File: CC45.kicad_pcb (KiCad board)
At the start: 2 copper layers, 247 x 80.8 mm, 130 parts, among them J1 AVR-ISP-6, SW1 RESET, SW10 K08, SW11 K09, SW12 K0A, SW13 K0B, SW14 K0C, SW15 K10, SW16 K11, SW17 K12, SW18 K13, SW19 K14, SW2 K00, SW20 K15, SW21 K16, SW22 K17, SW23 K18, SW24 K19, SW25 K1A, SW26 K1B, SW27 K20, SW28 K21, SW29 K22, SW3 K01, SW30 K23, SW31 K24, SW32 K25, SW33 K26, SW34 K27, SW35 K28, SW36 K29, SW37 K2A, SW38 K2B, SW39 K30, SW4 K02, SW40 K31, SW41 K32, SW42 K33, SW43 K34, SW44 K36, SW45 K38, SW46 K39, SW47 K3A, SW48 K3B, SW5 K03, SW6 K04, SW7 K05, SW8 K06, SW9 K07, U1 ATmega32U4-AU, U2 PRTR5V0U2X, X1 XTAL

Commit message: start adding rgb
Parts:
- removed G***: LOGO, cc:cc
- removed REF** (x5): MountingHole_2.2mm_M2_Pad, MountingHole:MountingHole_2.2mm_M2_Pad
- C1, C2, C3, C4, C5, C6, C7, C8: footprint custom:C_1206_3216Metric_Pad1.42x1.75mm_HandSolder -> Capacitor_SMD:C_1206_3216Metric_Pad1.42x1.75mm_HandSolder
- D1, D10, D11, D12, D13, D14, D15, D16, D17, D18, D19, D2, D20, D21, D22, D23, D24, D25, D26, D27, D28, D29, D3, D30, D31, D32, D33, D34, D35, D36, D37, D38, D39, D4, D40, D41, D42, D43, D44, D45, D46, D47, D5, D6, D7, D8, D9: footprint custom:D_SOD-323_HandSoldering -> Diode_SMD:D_SOD-323_HandSoldering
- R1, R2, R3, R4, R5, R6: footprint custom:R_1206_3216Metric_Pad1.42x1.75mm_HandSolder -> Resistor_SMD:R_1206_3216Metric_Pad1.42x1.75mm_HandSolder
- SW10, SW11, SW12, SW13, SW14, SW16, SW17, SW18, SW19, SW2, SW20, SW21, SW22, SW23, SW24, SW25, SW28, SW29, SW3, SW30, SW31, SW32, SW33, SW34, SW35, SW36, SW37, SW4, SW40 (x2), SW47 (x2), SW5, SW6, SW7, SW8, SW9: footprint MX_19mm:MX_19mm-1U-NoLED -> mx_rgb:ChocMx_Socket
- SW15, SW38, SW41, SW42, SW45: footprint MX_19mm:MX_19mm-1.25U-NoLED -> mx_rgb:ChocMx_Socket
- SW26, SW27, SW43, SW44: footprint MX_19mm:MX_19mm-1.75U-NoLED -> mx_rgb:ChocMx_Socket
- SW39, SW46, SW48: footprint MX_19mm:MX_19mm-1.25U-NoLED -> Button_Switch_Keyboard:SW_Cherry_MX_1.00u_PCB
- SW39, SW46, SW48: footprint MX_19mm:MX_19mm-1.5U-NoLED -> Button_Switch_Keyboard:SW_Cherry_MX_1.00u_PCB
- SW41: footprint MX_19mm:MX_19mm-1.5U-NoLED -> mx_rgb:ChocMx_Socket
- SW43: footprint MX_19mm:MX_19mm-2.25U-ReversedStabilizers-NoLED -> mx_rgb:ChocMx_Socket
- SW44: footprint MX_19mm:MX_19mm-2.75U-ReversedStabilizers-NoLED -> mx_rgb:ChocMx_Socket
- SW44: footprint MX_19mm:MX_19mm-6U-ReversedStabilizers-NoLED -> mx_rgb:ChocMx_Socket
- moved F1 5.29 mm to (156.5, 40.6)
- moved R6 4.01 mm to (152.1, 29.7), turned to 0 degrees
- moved R5 2.58 mm to (162.3, 29.0), turned to -90 degrees
- moved U2 1.39 mm to (158.0, 30.2)
- turned SW40 to 180 degrees
- turned SW8 to 180 degrees
- turned SW9 to 180 degrees
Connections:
- SW1 pad 1: RESET -> GND
- SW1 pad 2: GND -> RESET
- U1 pad 18: Net-(U1-Pad18) -> (no net)
- U1 pad 19: Net-(U1-Pad19) -> (no net)
- U1 pad 20: Net-(U1-Pad20) -> (no net)
- U1 pad 21: Net-(U1-Pad21) -> (no net)
- U1 pad 42: Net-(U1-Pad42) -> (no net)
- U1 pad 8: Net-(U1-Pad8) -> (no net)
- USB1 pad 3: Net-(USB1-Pad3) -> (no net)
- USB1 pad 9: Net-(USB1-Pad9) -> (no net)
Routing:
- net row0: track 404.0 -> 115.7 mm, vias 2 -> 0
- net row1: track 371.5 -> 109.0 mm, vias 2 -> 0
- net col11: track 184.4 -> 32.1 mm, vias 3 -> 0
- net col12: track 157.6 -> 10.4 mm, vias 3 -> 0
- net col10: track 158.8 -> 34.8 mm, vias 3 -> 0
- net col9: track 144.2 -> 38.5 mm, vias 3 -> 0
- net col8: track 125.7 -> 37.9 mm, vias 3 -> 0
- net GND: track 234.2 -> 149.0 mm, vias 2 -> 0
- net +5V: track 208.8 -> 144.5 mm, vias 9 -> 8
- net /USB_P: track 54.1 -> 2.89 mm
- net /USB_N: track 52.8 -> 3.04 mm
- net col6: track 84.8 -> 37.6 mm, vias 5 -> 3
- net col7: track 77.1 -> 33.2 mm
- net col2: track 129.4 -> 85.5 mm
- net col1: track 150.4 -> 106.5 mm
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
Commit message: routing
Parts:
- moved D8 1.78 mm to (174.5, 31.5)
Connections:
- D1 pad 1: row0 -> Net-(D1-Pad1)
- D10 pad 1: row0 -> Net-(D1-Pad1)
- D11 pad 1: row0 -> Net-(D1-Pad1)
- D12 pad 1: row0 -> Net-(D1-Pad1)
- D13 pad 1: row0 -> Net-(D1-Pad1)
- D2 pad 1: row0 -> Net-(D1-Pad1)
- D3 pad 1: row0 -> Net-(D1-Pad1)
- D4 pad 1: row0 -> Net-(D1-Pad1)
- D5 pad 1: row0 -> Net-(D1-Pad1)
- D6 pad 1: row0 -> Net-(D1-Pad1)
- D7 pad 1: row0 -> Net-(D1-Pad1)
- D8 pad 1: row0 -> Net-(D1-Pad1)
- D9 pad 1: row0 -> Net-(D1-Pad1)
- SW10 pad 1: Net-(D9-Pad2) -> Net-(SW10-Pad1)
- SW10 pad 10: (no net) -> Net-(SW10-Pad10)
- SW10 pad 11: (no net) -> Net-(SW10-Pad11)
- SW10 pad 12: (no net) -> Net-(SW10-Pad12)
- SW10 pad 2: col8 -> Net-(D9-Pad2)
- SW10 pad 9: (no net) -> Net-(SW10-Pad9)
- SW11 pad 1: Net-(D10-Pad2) -> Net-(SW10-Pad1)
- SW11 pad 10: (no net) -> Net-(SW10-Pad10)
- SW11 pad 11: (no net) -> Net-(SW10-Pad9)
- SW11 pad 12: (no net) -> Net-(SW10-Pad12)
- SW11 pad 2: col9 -> Net-(D10-Pad2)
- SW11 pad 9: (no net) -> Net-(SW11-Pad9)
- SW12 pad 1: Net-(D11-Pad2) -> Net-(SW10-Pad1)
- SW12 pad 10: (no net) -> Net-(SW10-Pad10)
- SW12 pad 11: (no net) -> Net-(SW11-Pad9)
- SW12 pad 12: (no net) -> Net-(SW10-Pad12)
- SW12 pad 2: col10 -> Net-(D11-Pad2)
- SW12 pad 9: (no net) -> Net-(SW12-Pad9)
- SW13 pad 1: Net-(D12-Pad2) -> Net-(SW10-Pad1)
- SW13 pad 10: (no net) -> Net-(SW10-Pad10)
- SW13 pad 11: (no net) -> Net-(SW12-Pad9)
- SW13 pad 12: (no net) -> Net-(SW10-Pad12)
- SW13 pad 2: col11 -> Net-(D12-Pad2)
- SW13 pad 9: (no net) -> Net-(SW13-Pad9)
- SW14 pad 1: Net-(D13-Pad2) -> Net-(SW10-Pad1)
- SW14 pad 10: (no net) -> Net-(SW10-Pad10)
- SW14 pad 11: (no net) -> Net-(SW13-Pad9)
- SW14 pad 12: (no net) -> Net-(SW10-Pad12)
- SW14 pad 2: col12 -> Net-(D13-Pad2)
- SW2 pad 1: Net-(D1-Pad2) -> Net-(SW10-Pad1)
- SW2 pad 10: (no net) -> Net-(SW10-Pad10)
- SW2 pad 12: (no net) -> Net-(SW10-Pad12)
- SW2 pad 2: col0 -> Net-(D1-Pad2)
- SW2 pad 9: (no net) -> Net-(SW2-Pad9)
- SW3 pad 1: Net-(D2-Pad2) -> Net-(SW10-Pad1)
- SW3 pad 10: (no net) -> Net-(SW10-Pad10)
- SW3 pad 11: (no net) -> Net-(SW2-Pad9)
- SW3 pad 12: (no net) -> Net-(SW10-Pad12)
- SW3 pad 2: col1 -> Net-(D2-Pad2)
- SW3 pad 9: (no net) -> Net-(SW3-Pad9)
- SW4 pad 1: Net-(D3-Pad2) -> Net-(SW10-Pad1)
- SW4 pad 10: (no net) -> Net-(SW10-Pad10)
- SW4 pad 11: (no net) -> Net-(SW3-Pad9)
- SW4 pad 12: (no net) -> Net-(SW10-Pad12)
- SW4 pad 2: col2 -> Net-(D3-Pad2)
- SW4 pad 9: (no net) -> Net-(SW4-Pad9)
- SW5 pad 1: Net-(D4-Pad2) -> Net-(SW10-Pad1)
- SW5 pad 10: (no net) -> Net-(SW10-Pad10)
- SW5 pad 11: (no net) -> Net-(SW4-Pad9)
- SW5 pad 12: (no net) -> Net-(SW10-Pad12)
- SW5 pad 2: col3 -> Net-(D4-Pad2)
- SW5 pad 9: (no net) -> Net-(SW5-Pad9)
- SW6 pad 1: Net-(D5-Pad2) -> Net-(SW10-Pad1)
- SW6 pad 10: (no net) -> Net-(SW10-Pad10)
- SW6 pad 11: (no net) -> Net-(SW5-Pad9)
- SW6 pad 12: (no net) -> Net-(SW10-Pad12)
- SW6 pad 2: col4 -> Net-(D5-Pad2)
- SW6 pad 9: (no net) -> Net-(SW6-Pad9)
- SW7 pad 1: Net-(D6-Pad2) -> Net-(SW10-Pad1)
- SW7 pad 10: (no net) -> Net-(SW10-Pad10)
- SW7 pad 11: (no net) -> Net-(SW6-Pad9)
- SW7 pad 12: (no net) -> Net-(SW10-Pad12)
- SW7 pad 2: col5 -> Net-(D6-Pad2)
- SW7 pad 9: (no net) -> Net-(SW7-Pad9)
- SW8 pad 1: Net-(D7-Pad2) -> Net-(SW10-Pad1)
- SW8 pad 10: (no net) -> Net-(SW10-Pad10)
- SW8 pad 11: (no net) -> Net-(SW7-Pad9)
- SW8 pad 12: (no net) -> Net-(SW10-Pad12)
- SW8 pad 2: col6 -> Net-(D7-Pad2)
- SW8 pad 9: (no net) -> Net-(SW8-Pad9)
- SW9 pad 1: Net-(D8-Pad2) -> Net-(SW10-Pad1)
- SW9 pad 10: (no net) -> Net-(SW10-Pad10)
- SW9 pad 11: (no net) -> Net-(SW8-Pad9)
- SW9 pad 12: (no net) -> Net-(SW10-Pad12)
- SW9 pad 2: col7 -> Net-(D8-Pad2)
- SW9 pad 9: (no net) -> Net-(SW10-Pad11)
- U1 pad 25: row0 -> (no net)
- U1 pad 41: col12 -> (no net)
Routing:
- net Net-(D1-Pad1): track 0.00 -> 272.2 mm, vias 0 -> 13
- net Net-(SW10-Pad12): track 0.00 -> 219.4 mm, vias 0 -> 11
- net Net-(SW10-Pad10): track 0.00 -> 195.2 mm, vias 0 -> 11
- net Net-(SW10-Pad1): track 0.00 -> 164.8 mm
- net row0: track 115.7 -> 0.00 mm
- net col0: track 128.9 -> 243.9 mm
- net /USB_N: track 3.04 -> 52.2 mm, vias 0 -> 2
- net GND: track 149.0 -> 184.5 mm
- net VCC: track 0.00 -> 31.3 mm, vias 0 -> 3
- net Net-(D8-Pad2): track 0.00 -> 26.6 mm
- net Net-(SW13-Pad9): track 0.00 -> 19.6 mm
- net Net-(SW6-Pad9): track 0.00 -> 19.6 mm
- net Net-(SW5-Pad9): track 0.00 -> 19.6 mm
- net Net-(SW4-Pad9): track 0.00 -> 19.6 mm
- net Net-(SW3-Pad9): track 0.00 -> 19.6 mm
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
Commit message: 2d line on schem
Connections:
- D14 pad 2: Net-(D14-Pad2) -> (no net)
- D15 pad 2: Net-(D15-Pad2) -> (no net)
- D16 pad 2: Net-(D16-Pad2) -> (no net)
- D17 pad 2: Net-(D17-Pad2) -> (no net)
- D18 pad 2: Net-(D18-Pad2) -> (no net)
- D19 pad 2: Net-(D19-Pad2) -> (no net)
- D20 pad 2: Net-(D20-Pad2) -> (no net)
- D21 pad 2: Net-(D21-Pad2) -> (no net)
- D22 pad 2: Net-(D22-Pad2) -> (no net)
- D23 pad 2: Net-(D23-Pad2) -> (no net)
- D24 pad 2: Net-(D24-Pad2) -> (no net)
- D25 pad 2: Net-(D25-Pad2) -> (no net)
- SW10 pad 1: Net-(SW10-Pad1) -> (no net)
- SW11 pad 1: Net-(SW10-Pad1) -> (no net)
- SW12 pad 1: Net-(SW10-Pad1) -> (no net)
- SW13 pad 1: Net-(SW10-Pad1) -> (no net)
- SW14 pad 1: Net-(SW10-Pad1) -> (no net)
- SW15 pad 1: Net-(D14-Pad2) -> (no net)
- SW15 pad 2: col0 -> (no net)
- SW16 pad 1: Net-(D15-Pad2) -> (no net)
- SW16 pad 2: col1 -> (no net)
- SW17 pad 1: Net-(D16-Pad2) -> (no net)
- SW17 pad 2: col2 -> (no net)
- SW18 pad 1: Net-(D17-Pad2) -> (no net)
- SW18 pad 2: col3 -> (no net)
- SW19 pad 1: Net-(D18-Pad2) -> (no net)
- SW19 pad 2: col4 -> (no net)
- SW2 pad 1: Net-(SW10-Pad1) -> (no net)
- SW20 pad 1: Net-(D19-Pad2) -> (no net)
- SW20 pad 2: col5 -> (no net)
- SW21 pad 1: Net-(D20-Pad2) -> (no net)
- SW21 pad 2: col6 -> (no net)
- SW22 pad 1: Net-(D21-Pad2) -> (no net)
- SW22 pad 2: col7 -> (no net)
- SW23 pad 1: Net-(D22-Pad2) -> (no net)
- SW23 pad 2: col8 -> (no net)
- SW24 pad 1: Net-(D23-Pad2) -> (no net)
- SW24 pad 2: col9 -> (no net)
- SW25 pad 1: Net-(D24-Pad2) -> (no net)
- SW25 pad 2: col10 -> (no net)
- SW26 pad 1: Net-(D25-Pad2) -> (no net)
- SW26 pad 2: col11 -> (no net)
- SW3 pad 1: Net-(SW10-Pad1) -> (no net)
- SW4 pad 1: Net-(SW10-Pad1) -> (no net)
- SW5 pad 1: Net-(SW10-Pad1) -> (no net)
- SW6 pad 1: Net-(SW10-Pad1) -> (no net)
- SW7 pad 1: Net-(SW10-Pad1) -> (no net)
- SW8 pad 1: Net-(SW10-Pad1) -> (no net)
- SW9 pad 1: Net-(SW10-Pad1) -> (no net)
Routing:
- net Net-(SW10-Pad1): track 164.8 -> 0.00 mm
- net Net-(SW10-Pad10): track 195.2 -> 278.4 mm, vias 11 -> 13
- net Net-(SW10-Pad12): track 219.4 -> 292.4 mm, vias 11 -> 15
- net GND: track 184.5 -> 224.2 mm, vias 0 -> 1
- net VCC: track 31.3 -> 64.0 mm, vias 3 -> 4
- net Net-(SW8-Pad9): track 0.00 -> 29.1 mm, vias 0 -> 2
- net Net-(SW10-Pad11): track 0.00 -> 28.9 mm, vias 0 -> 2
- net Net-(SW7-Pad9): track 0.00 -> 28.3 mm, vias 0 -> 2
- net /USB_P: track 10.6 -> 38.3 mm
- net Net-(D1-Pad1): track 272.2 -> 273.4 mm, vias 13 -> 15
- net /USB_N: track 52.2 -> 51.2 mm, vias 2 -> 1

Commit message: moar routing
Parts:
- removed J1: AVR-ISP-6, random-keyboard-parts:Reset_Pretty-Mask
- moved D30 16.1 mm to (116.8, 64.3), turned to -90 degrees
- moved D24 11.9 mm to (227.3, 44.4)
- moved D20 5.92 mm to (143.7, 58.2)
- moved D31 5.61 mm to (135.1, 64.5), turned to -90 degrees
- moved U1 1.74 mm to (145.8, 83.1), turned to -135 degrees
- moved D42 1.45 mm to (113.3, 91.7)
- moved D19 0.09 mm to (141.2, 52.2)
- turned SW32 to 180 degrees
- turned SW47 to 180 degrees
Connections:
- C2 pad 1: +5V -> Vcc
- C3 pad 1: +5V -> Vcc
- C4 pad 1: +5V -> Vcc
- C5 pad 1: +5V -> Vcc
- C8 pad 1: +5V -> Vcc
- D1 pad 1: Net-(D1-Pad1) -> row0
- D10 pad 1: Net-(D1-Pad1) -> row0
- D11 pad 1: Net-(D1-Pad1) -> row0
- D12 pad 1: Net-(D1-Pad1) -> row0
- D13 pad 1: Net-(D1-Pad1) -> row0
- D14 pad 2: (no net) -> Net-(D14-Pad2)
- D15 pad 2: (no net) -> Net-(D15-Pad2)
- D16 pad 2: (no net) -> Net-(D16-Pad2)
- D17 pad 2: (no net) -> Net-(D17-Pad2)
- D18 pad 2: (no net) -> Net-(D18-Pad2)
- D19 pad 2: (no net) -> Net-(D19-Pad2)
- D2 pad 1: Net-(D1-Pad1) -> row0
- D20 pad 2: (no net) -> Net-(D20-Pad2)
- D21 pad 2: (no net) -> Net-(D21-Pad2)
- D22 pad 2: (no net) -> Net-(D22-Pad2)
- D23 pad 2: (no net) -> Net-(D23-Pad2)
- D24 pad 2: (no net) -> Net-(D24-Pad2)
- D25 pad 2: (no net) -> Net-(D25-Pad2)
- D3 pad 1: Net-(D1-Pad1) -> row0
- D4 pad 1: Net-(D1-Pad1) -> row0
- D5 pad 1: Net-(D1-Pad1) -> row0
- D6 pad 1: Net-(D1-Pad1) -> row0
- D7 pad 1: Net-(D1-Pad1) -> row0
- D8 pad 1: Net-(D1-Pad1) -> row0
- D9 pad 1: Net-(D1-Pad1) -> row0
- F1 pad 1: +5V -> Vcc
- R4 pad 2: +5V -> Vcc
- SW10 pad 1: (no net) -> col8
- SW10 pad 10: Net-(SW10-Pad10) -> Vcc
- SW10 pad 12: Net-(SW10-Pad12) -> GND
- SW11 pad 1: (no net) -> col9
- SW11 pad 10: Net-(SW10-Pad10) -> Vcc
- SW11 pad 12: Net-(SW10-Pad12) -> GND
- SW12 pad 1: (no net) -> col10
- SW12 pad 10: Net-(SW10-Pad10) -> Vcc
- SW12 pad 12: Net-(SW10-Pad12) -> GND
- SW13 pad 1: (no net) -> col11
- SW13 pad 10: Net-(SW10-Pad10) -> Vcc
- SW13 pad 12: Net-(SW10-Pad12) -> GND
- SW14 pad 1: (no net) -> col12
- SW14 pad 10: Net-(SW10-Pad10) -> Vcc
- SW14 pad 12: Net-(SW10-Pad12) -> GND
- SW14 pad 9: (no net) -> Net-(SW14-Pad9)
- SW15 pad 1: (no net) -> col0
- SW15 pad 10: (no net) -> Vcc
- SW15 pad 11: (no net) -> Net-(SW14-Pad9)
- SW15 pad 12: (no net) -> GND
- SW15 pad 2: (no net) -> Net-(D14-Pad2)
- SW15 pad 9: (no net) -> Net-(SW15-Pad9)
- SW16 pad 1: (no net) -> col1
- SW16 pad 10: (no net) -> Vcc
- SW16 pad 11: (no net) -> Net-(SW15-Pad9)
- SW16 pad 12: (no net) -> GND
- SW16 pad 2: (no net) -> Net-(D15-Pad2)
- SW16 pad 9: (no net) -> Net-(SW16-Pad9)
- SW17 pad 1: (no net) -> Net-(SW17-Pad1)
- SW17 pad 10: (no net) -> Vcc
- SW17 pad 11: (no net) -> Net-(SW16-Pad9)
- SW17 pad 12: (no net) -> GND
- SW17 pad 2: (no net) -> Net-(D16-Pad2)
- SW17 pad 9: (no net) -> Net-(SW17-Pad9)
- SW18 pad 1: (no net) -> col3
- SW18 pad 10: (no net) -> Vcc
- SW18 pad 11: (no net) -> Net-(SW17-Pad9)
- SW18 pad 12: (no net) -> GND
- SW18 pad 2: (no net) -> Net-(D17-Pad2)
- SW18 pad 9: (no net) -> Net-(SW18-Pad9)
- SW19 pad 1: (no net) -> col4
- SW19 pad 10: (no net) -> Vcc
- SW19 pad 11: (no net) -> Net-(SW18-Pad9)
- SW19 pad 12: (no net) -> GND
- SW19 pad 2: (no net) -> Net-(D18-Pad2)
- SW19 pad 9: (no net) -> Net-(SW19-Pad9)
- SW2 pad 1: (no net) -> col0
- SW2 pad 10: Net-(SW10-Pad10) -> Vcc
- SW2 pad 12: Net-(SW10-Pad12) -> GND
- SW20 pad 1: (no net) -> col5
- SW20 pad 10: (no net) -> Vcc
- SW20 pad 11: (no net) -> Net-(SW19-Pad9)
- SW20 pad 12: (no net) -> GND
- SW20 pad 2: (no net) -> Net-(D19-Pad2)
- SW20 pad 9: (no net) -> Net-(SW20-Pad9)
- SW21 pad 1: (no net) -> col6
- SW21 pad 10: (no net) -> Vcc
- SW21 pad 11: (no net) -> Net-(SW20-Pad9)
- SW21 pad 12: (no net) -> GND
- SW21 pad 2: (no net) -> Net-(D20-Pad2)
- SW21 pad 9: (no net) -> Net-(SW21-Pad9)
- SW22 pad 1: (no net) -> col7
- SW22 pad 10: (no net) -> Vcc
- SW22 pad 11: (no net) -> Net-(SW21-Pad9)
- SW22 pad 12: (no net) -> GND
- SW22 pad 2: (no net) -> Net-(D21-Pad2)
- SW22 pad 9: (no net) -> Net-(SW22-Pad9)
- SW23 pad 1: (no net) -> col8
- SW23 pad 10: (no net) -> Vcc
- SW23 pad 11: (no net) -> Net-(SW22-Pad9)
- SW23 pad 12: (no net) -> GND
- SW23 pad 2: (no net) -> Net-(D22-Pad2)
- SW23 pad 9: (no net) -> Net-(SW23-Pad9)
- SW24 pad 1: (no net) -> col9
- SW24 pad 10: (no net) -> Vcc
- SW24 pad 11: (no net) -> Net-(SW23-Pad9)
- SW24 pad 12: (no net) -> GND
- SW24 pad 2: (no net) -> Net-(D23-Pad2)
- SW24 pad 9: (no net) -> Net-(SW24-Pad9)
- SW25 pad 1: (no net) -> col10
- SW25 pad 10: (no net) -> Vcc
- SW25 pad 11: (no net) -> Net-(SW24-Pad9)
- SW25 pad 12: (no net) -> GND
- SW25 pad 2: (no net) -> Net-(D24-Pad2)
- SW25 pad 9: (no net) -> Net-(SW25-Pad9)
- SW26 pad 1: (no net) -> col11
- SW26 pad 10: (no net) -> Vcc
- SW26 pad 11: (no net) -> Net-(SW25-Pad9)
- SW26 pad 12: (no net) -> GND
- SW26 pad 2: (no net) -> Net-(D25-Pad2)
- SW3 pad 1: (no net) -> col1
- SW3 pad 10: Net-(SW10-Pad10) -> Vcc
- SW3 pad 12: Net-(SW10-Pad12) -> GND
- SW4 pad 1: (no net) -> Net-(SW17-Pad1)
- SW4 pad 10: Net-(SW10-Pad10) -> Vcc
- SW4 pad 12: Net-(SW10-Pad12) -> GND
- SW5 pad 1: (no net) -> col3
- SW5 pad 10: Net-(SW10-Pad10) -> Vcc
- SW5 pad 12: Net-(SW10-Pad12) -> GND
- SW6 pad 1: (no net) -> col4
- SW6 pad 10: Net-(SW10-Pad10) -> Vcc
- SW6 pad 12: Net-(SW10-Pad12) -> GND
- SW7 pad 1: (no net) -> col5
- SW7 pad 10: Net-(SW10-Pad10) -> Vcc
- SW7 pad 12: Net-(SW10-Pad12) -> GND
- SW8 pad 1: (no net) -> col6
- SW8 pad 10: Net-(SW10-Pad10) -> Vcc
- SW8 pad 12: Net-(SW10-Pad12) -> GND
- SW9 pad 1: (no net) -> col7
- SW9 pad 10: Net-(SW10-Pad10) -> Vcc
- SW9 pad 12: Net-(SW10-Pad12) -> GND
- U1 pad 14: +5V -> Vcc
- U1 pad 2: +5V -> Vcc
- U1 pad 24: +5V -> Vcc
- U1 pad 25: (no net) -> row0
- U1 pad 34: +5V -> Vcc
- U1 pad 41: (no net) -> col12
- U1 pad 44: +5V -> Vcc
- U1 pad 7: +5V -> Vcc
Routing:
- net Vcc: track 0.00 -> 508.3 mm, vias 0 -> 25
- net GND: track 224.2 -> 604.7 mm, vias 1 -> 30
- net row2: track 307.5 -> 0.00 mm
- net Net-(SW10-Pad12): track 292.4 -> 0.00 mm, vias 15 -> 0
- net Net-(SW10-Pad10): track 278.4 -> 0.00 mm, vias 13 -> 0
- net row0: track 0.00 -> 273.8 mm, vias 0 -> 16
- net Net-(D1-Pad1): track 273.4 -> 0.00 mm, vias 15 -> 0
- net row3: track 262.2 -> 0.00 mm, vias 4 -> 0
- net col0: track 243.9 -> 48.6 mm, vias 1 -> 0
- net +5V: track 144.5 -> 0.00 mm, vias 8 -> 0
- net row1: track 109.0 -> 219.8 mm, vias 0 -> 11
- net col2: track 85.5 -> 0.00 mm, vias 1 -> 0
- net col1: track 106.5 -> 57.1 mm, vias 1 -> 4
- net RESET: track 46.4 -> 0.00 mm
- net col5: track 8.90 -> 53.5 mm, vias 0 -> 4
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- removed copper zone on B.Cu, net GND

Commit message: who needs MCUs anyway
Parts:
- removed C2, C3, C4, C8: 0.1u, Capacitor_SMD:C_1206_3216Metric_Pad1.42x1.75mm_HandSolder
- removed C6, C7: 22p, Capacitor_SMD:C_1206_3216Metric_Pad1.42x1.75mm_HandSolder
- removed R1: 10k, Resistor_SMD:R_1206_3216Metric_Pad1.42x1.75mm_HandSolder
- removed U1: ATmega32U4-AU, Package_QFP:TQFP-44_10x10mm_P0.8mm
- removed X1: XTAL, Crystal:Crystal_SMD_3225-4Pin_3.2x2.5mm_HandSoldering
- SW39 (x2), SW46 (x2), SW48 (x2): footprint Button_Switch_Keyboard:SW_Cherry_MX_1.00u_PCB -> mx_rgb:ChocMx_Socket
- turned SW39 to 180 degrees
- turned SW48 to 180 degrees

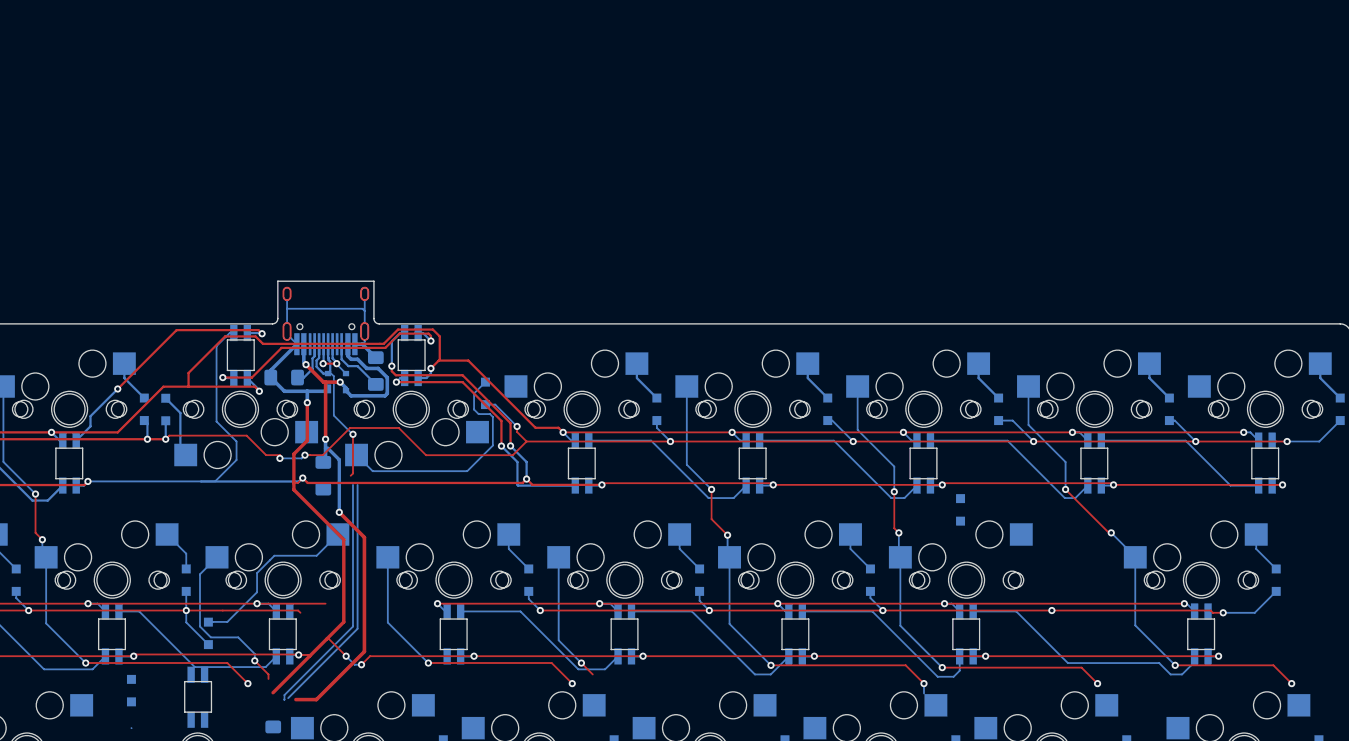
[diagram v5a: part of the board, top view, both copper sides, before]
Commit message: add socket keep out zones
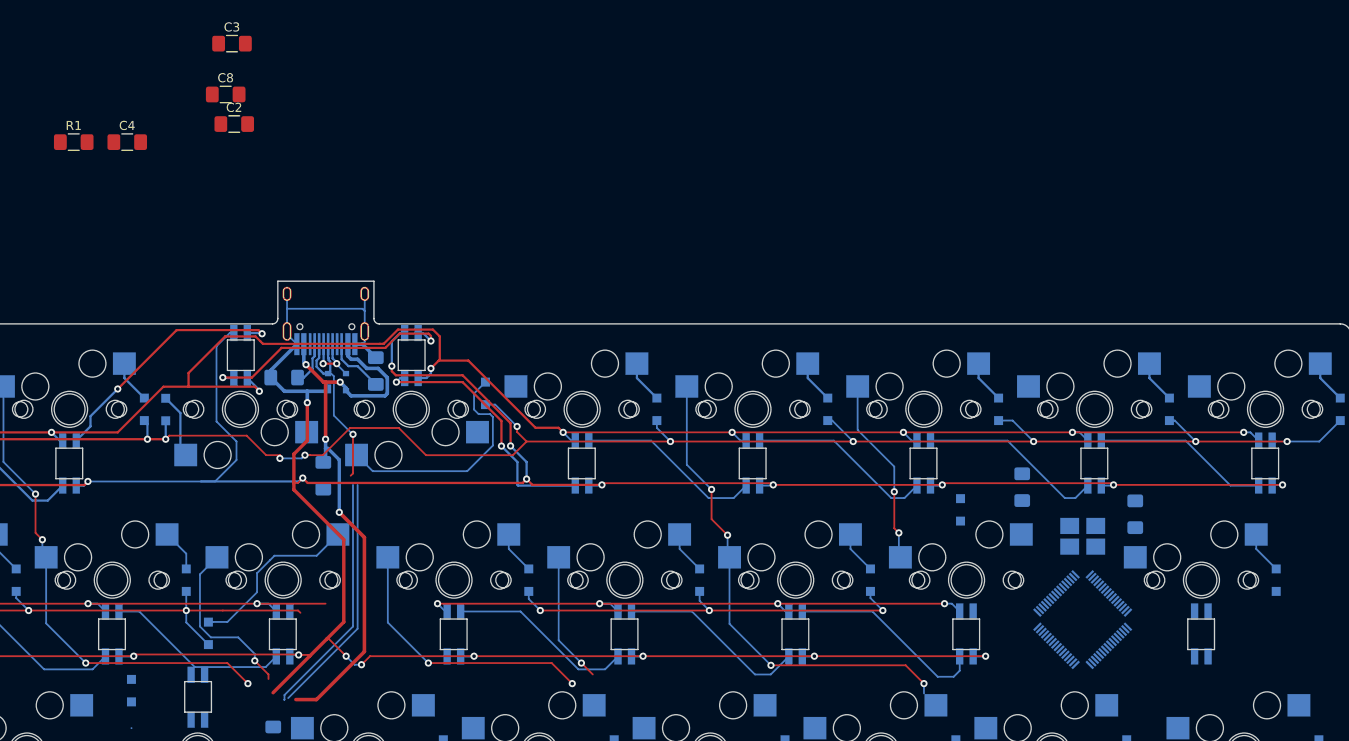
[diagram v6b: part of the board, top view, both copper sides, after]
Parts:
- added C2: 0.1u, Capacitor_SMD:C_1206_3216Metric_Pad1.42x1.75mm_HandSolder, F.Cu at (146.6, 1.52)
- added C3: 0.1u, Capacitor_SMD:C_1206_3216Metric_Pad1.42x1.75mm_HandSolder, F.Cu at (146.3, -7.42)
- added C4: 0.1u, Capacitor_SMD:C_1206_3216Metric_Pad1.42x1.75mm_HandSolder, F.Cu at (134.7, 3.53)
- added C6: 22p, Capacitor_SMD:C_1206_3216Metric_Pad1.42x1.75mm_HandSolder, B.Cu at (246.8, 44.9)
- added C7: 22p, Capacitor_SMD:C_1206_3216Metric_Pad1.42x1.75mm_HandSolder, B.Cu at (234.2, 41.9)
- added C8: 0.1u, Capacitor_SMD:C_1206_3216Metric_Pad1.42x1.75mm_HandSolder, F.Cu at (145.6, -1.77)
- added R1: 10k, Resistor_SMD:R_1206_3216Metric_Pad1.42x1.75mm_HandSolder, F.Cu at (128.7, 3.53)
- added U1: ATmega32U4-AU, Package_QFP:TQFP-64_7x7mm_P0.4mm, B.Cu at (240.9, 56.6)
- added X1: XTAL, Crystal:Crystal_SMD_3225-4Pin_3.2x2.5mm_HandSoldering, B.Cu at (240.9, 47.4)
- SW44: footprint mx_rgb:ChocMx_Socket -> mx_rgb:mx_with_stabilizer
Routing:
- net col11: track 51.7 -> 0.00 mm, vias 4 -> 0
- net row1: track 219.8 -> 174.9 mm, vias 11 -> 9
- net col10: track 53.2 -> 21.0 mm, vias 4 -> 2
- net Net-(SW25-Pad9): track 28.7 -> 0.00 mm
- net Vcc: track 508.3 -> 480.1 mm, vias 25 -> 24
- net GND: track 604.7 -> 577.6 mm, vias 30 -> 29
